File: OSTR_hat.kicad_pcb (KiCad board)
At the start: 4 copper layers, 65 x 56 mm, 87 parts, among them J1 GPIO, J10 PWM4, J11 PWM5, J13 Servo17, J14 Servo6, J16 1Wire, J17 I2C0, J18 I2C1, J19 3.3V, J2 ADC_IN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

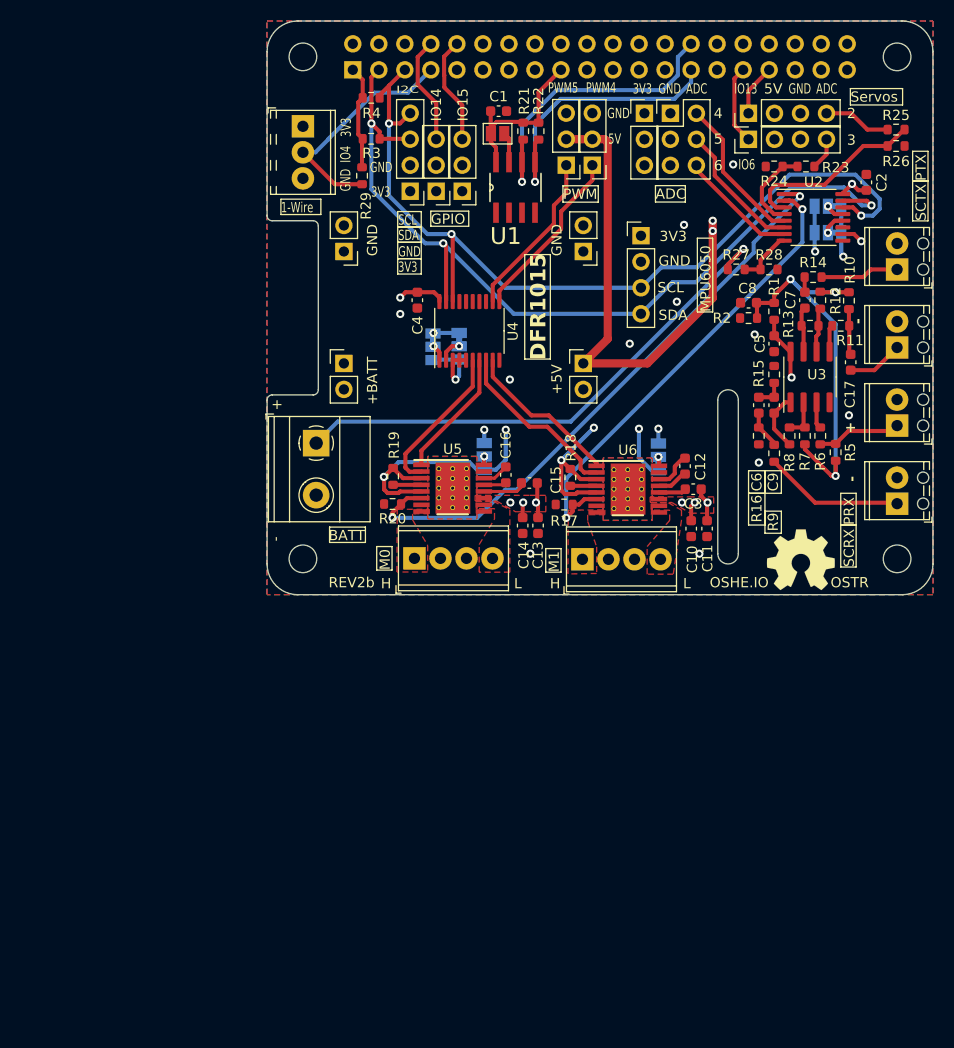
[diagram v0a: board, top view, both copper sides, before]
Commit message: Added stackup and description to PCB design
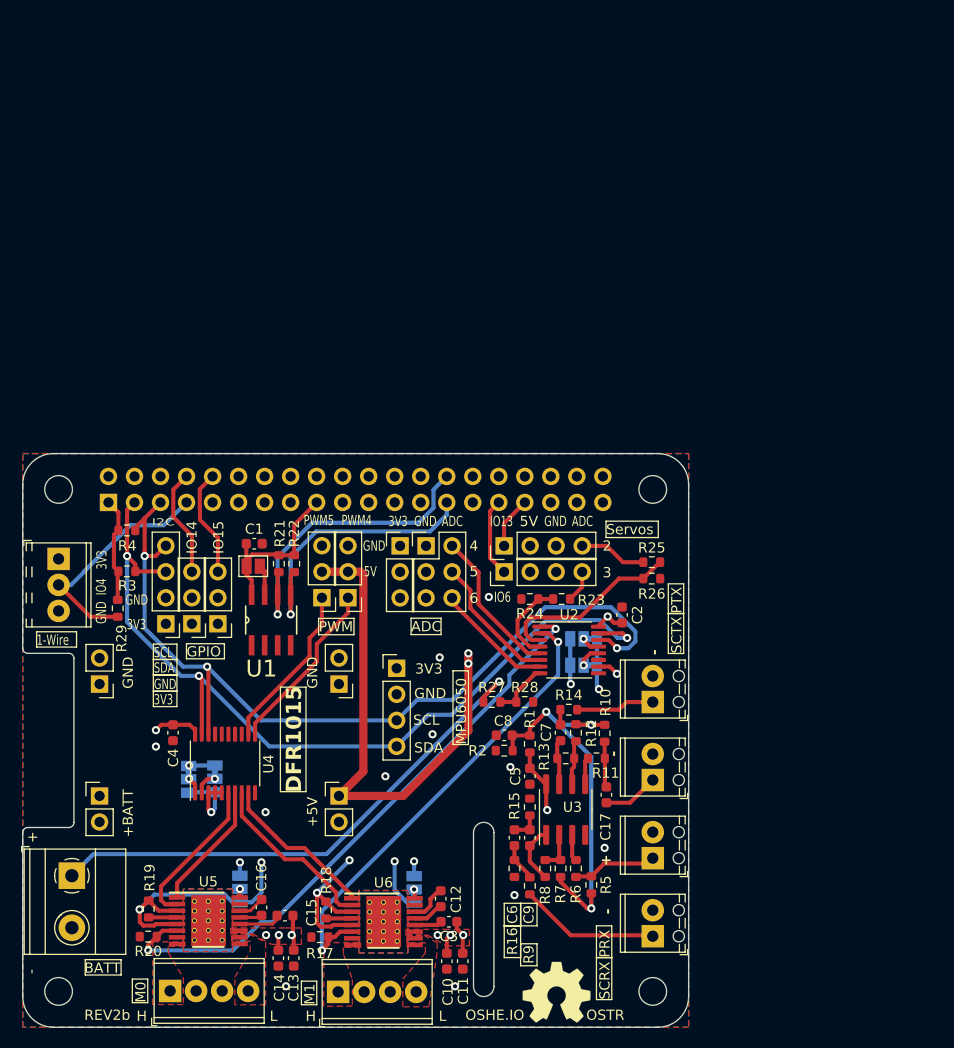
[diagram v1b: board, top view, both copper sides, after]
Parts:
- moved R10 48.5 mm to (132.9, 113.5)
- moved C1 48.5 mm to (98.8, 95.0)
- moved C10 48.5 mm to (117.5, 135.8)
- moved C11 48.5 mm to (119.1, 135.8)
- moved C12 48.5 mm to (117.0, 129.7)
- moved C3 48.5 mm to (117.8, 131.9)
- moved J14 48.5 mm to (123.1, 97.8)
- moved J17 48.5 mm to (112.7, 107.2)
- moved J21 48.5 mm to (83.7, 119.6)
- moved J23 48.5 mm to (107.0, 119.6)
- moved J3 48.5 mm to (90.5, 138.7)
- moved J5 48.5 mm to (106.9, 138.8)
- moved J7 48.5 mm to (137.7, 133.3)
- moved J8 48.5 mm to (137.7, 110.5)
- moved J9 48.5 mm to (80.9, 127.4)
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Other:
- board text added: "Raspberry Pi HAT capabilities: * Can drive two bidirectional 12 V DC motors or four unidirectional 12 V DC motors * Can control up to two 5 V servos and read from the feedback potentiometer if it's broken out of the servo. These headers can also be used as 5 V ADC inputs * Has three 3.3 V ADC headers with 3.3 V and GND available. Can be used to read from a potentiometer. * Two 3.3 V PWM headers w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"
